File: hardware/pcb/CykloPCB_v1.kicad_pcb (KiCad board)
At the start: 2 copper layers, 43 x 64 mm, 44 parts, among them J1 USB-C 16P, J2 TFT, J3 GPS, J4 LiPo 3.7V, J5 BTN ext, Q1 AO3401A, Q2 AO3401A, Q3 AO3401A, SW1 ON/OFF, SW2 MODE, SW3 START, SW4 PAUSE, U1 TP4056, U2 AP2112K-3.3, U3 ESP32-C3-Zero

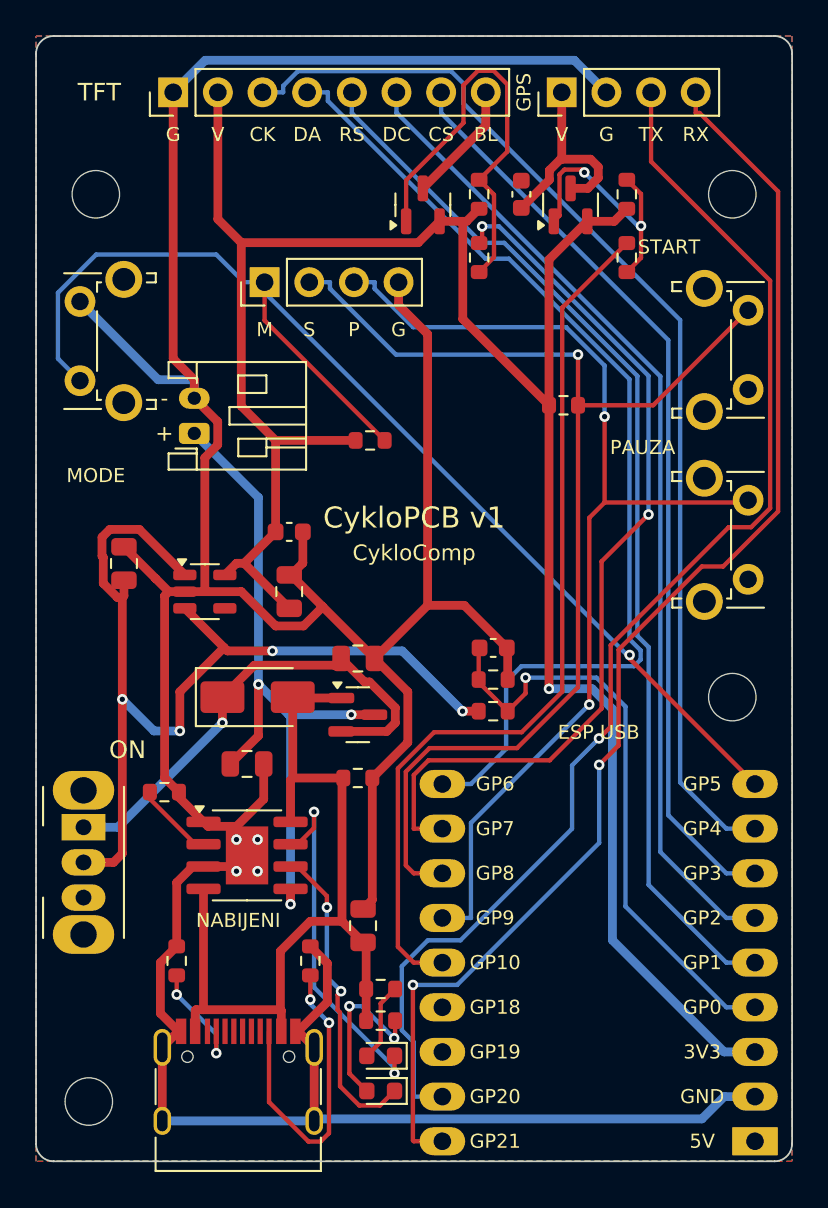
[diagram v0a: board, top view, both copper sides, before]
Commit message: PCB: fix JLCPCB DFM findings (slots, vias, EP vias, silkscreen, mask)
- USB-C shield slots 0.6 -> 0.7 mm (slot width check)
- vias 0.6/0.3 -> 0.7/0.3, 0.2 mm annular ring
- TP4056 exposed-pad GND vias moved out of the pad, tied with 0.5 mm stubs
- Freerouting keeps vias >= 0.3 mm from SMD pads; LED column moved to x=18.5
- silkscreen >= 0.16 mm, clipped >= 0.25 mm from holes and 0.2 mm from
  pad openings and board edge; pin-1 marks and texts nudged clear
- solder mask +0.05 mm (USB-C +0.025), no stacked openings on USB-C pads
- generator refuses to write fab outputs for a dirty board (--force)

Co-Authored-By: Claude Opus 5.5 <noreply@anthropic.com>
Claude-Session: https://claude.ai/code/session_01U4G6Wqkxv8dALXYEZtDemh
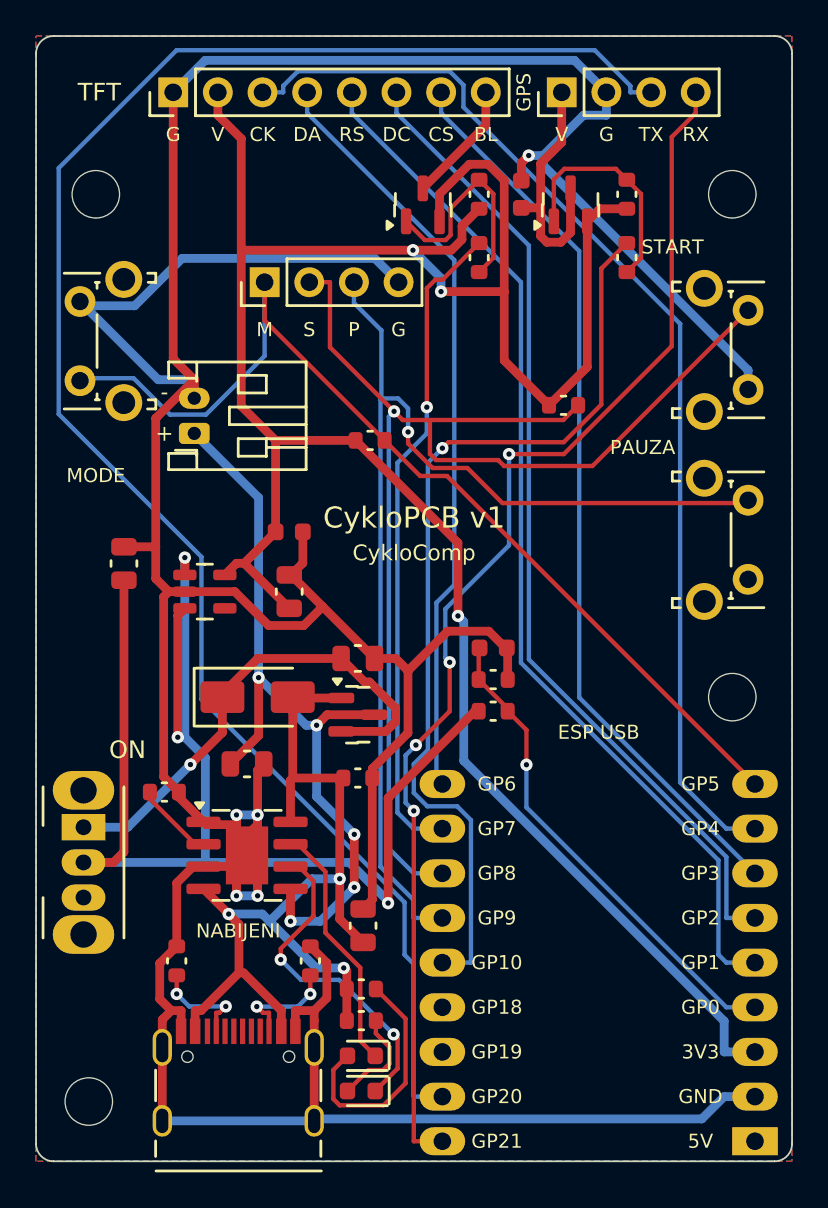
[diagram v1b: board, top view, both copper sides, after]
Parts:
- moved D1 1.10 mm to (18.5, 58.0)
- moved D2 1.10 mm to (18.5, 60.0)
- moved R4 1.10 mm to (18.5, 54.2)
- moved R5 1.10 mm to (18.5, 56.0)
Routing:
- net GND: track 225.5 -> 260.8 mm, vias 4 -> 5
- net GPS_TXD: track 72.3 -> 100.5 mm, vias 1 -> 0
- net VSW: track 57.0 -> 76.2 mm, vias 4 -> 3
- net 3V3: track 123.3 -> 139.3 mm, vias 1 -> 3
- net TFT_MOSI: track 58.0 -> 43.4 mm
- net BL_PWM: track 51.0 -> 37.5 mm, vias 2 -> 1
- net BTN1: track 71.1 -> 58.0 mm, vias 1 -> 0
- net CC2: track 18.0 -> 6.30 mm
- net BL_G: track 24.3 -> 12.8 mm
- net LED_R: track 4.47 -> 13.6 mm
- net BTN2: track 67.4 -> 73.6 mm
- net BAT_SENSE: track 34.1 -> 27.9 mm
- net CHRG: track 20.4 -> 14.3 mm, vias 2 -> 0
- net BAT+: track 39.9 -> 45.3 mm, vias 3 -> 5
- net VBUS: track 48.9 -> 53.3 mm, vias 0 -> 3
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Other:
- rule pad_to_mask_clearance: 0 -> 0.05
